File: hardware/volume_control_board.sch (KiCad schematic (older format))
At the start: 39 parts, among them J1 Screw_Terminal_01x08, J2 Audio-Jack-3, J3 Conn_01x04, J4 Conn_01x04, J5 Conn_01x04, J6 RXTX/CAN, SW1 Rotary_Encoder_Switch, U1 Teensy3.2, U2 AD5254

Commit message: finished first draft.
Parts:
- removed J2: Audio-Jack-3, project:BARREL_JACK, symbol volume_control_board-rescue:Audio-Jack-3
- removed SW1: Rotary_Encoder_Switch, Rotary_Encoder:RotaryEncoder_Alps_EC11E-Switch_Vertical_H20mm, symbol volume_control_board-rescue:Rotary_Encoder_Switch
- added J2: AudioJack3, Connector_Audio:Jack_3.5mm_CUI_SJ-3523-SMT_Horizontal, symbol Connector:AudioJack3
- added SW1: Rotary_Encoder_Switch, Rotary_Encoder:RotaryEncoder_Alps_EC11E-Switch_Vertical_H20mm, symbol Device:Rotary_Encoder_Switch
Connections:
- net GND: now also SW1.C, SW1.S2
- net GNDA: now also J2.S
- net LEFT_IN: now also J2.T; no longer J4.1 (Pin_1), U2.1 (W0), U2.2 (B0)
- net RIGHT_IN: now also J2.R; no longer J4.3 (Pin_3), U2.12 (B2), U2.13 (W2)
- net at J3.1 (Pin_1), R4.2, R6.2: now also SW1.A
- net at J3.2 (Pin_2), R5.1, R7.2: now also SW1.B
- net at J3.3 (Pin_3), R8.2, R9.2: now also SW1.S1
- new net: J4.1 (Pin_1), U2.1 (W0), U2.2 (B0)
- new net: J4.3 (Pin_3), U2.12 (B2), U2.13 (W2)
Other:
- moved on the sheet: C5
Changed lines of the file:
@@
-$EndComp
-$Comp
-L volume_control_board-rescue:Rotary_Encoder_Switch SW1
-U 1 1 5C4E5A09
-P 7350 5600
-F 0 "SW1" H 7350 5860 50  0000 C CNN
-F 1 "Rotary_Encoder_Switch" H 7350 5340 50  0000 C CNN
-F 2 "Rotary_Encoder:RotaryEncoder_Alps_EC11E-Switch_Vertical_H20mm" H 7250 5760 50  0001 C CNN
-F 3 "" H 7350 5860 50  0001 C CNN
-	1    7350 5600
-	1    0    0    -1
 $EndComp
 $Comp
@@
 Text Notes 5250 2050 0    59   ~ 0
 Digital Potentiometer
-Text GLabel 8300 4050 0    39   Input ~ 0
+Text GLabel 8800 4150 2    39   Input ~ 0
 RIGHT_IN
-Text GLabel 8300 3950 0    39   Input ~ 0
+Text GLabel 8800 4250 2    39   Input ~ 0
 LEFT_IN
-$Comp
-L volume_control_board-rescue:Audio-Jack-3 J2
-U 1 1 5C526FE2
-P 8600 3950
-F 0 "J2" H 8550 4125 50  0000 C CNN
-F 1 "Audio-Jack-3" H 8700 3850 50  0000 C CNN
-F 2 "project:BARREL_JACK" H 8850 4050 50  0001 C CNN
-F 3 "" H 8850 4050 50  0001 C CNN
-	1    8600 3950
-	-1   0    0    1
-$EndComp
 $Comp
 L volume_control_board-rescue:C C5
 U 1 1 5C527180
-P 9550 3950
-F 0 "C5" H 9575 4050 50  0000 L CNN
-F 1 "0.1uF" H 9575 3850 50  0000 L CNN
-F 2 "Capacitors_SMD:C_0805" H 9588 3800 50  0001 C CNN
-F 3 "" H 9550 3950 50  0001 C CNN
-	1    9550 3950
+P 9500 4150
+F 0 "C5" H 9525 4250 50  0000 L CNN
+F 1 "0.1uF" H 9525 4050 50  0000 L CNN
+F 2 "Capacitors_SMD:C_0805" H 9538 4000 50  0001 C CNN
+F 3 "" H 9500 4150 50  0001 C CNN
+	1    9500 4150
 	1    0    0    -1
 $EndComp
@@
 L power:GND #PWR022
 U 1 1 5C527214
-P 9550 4150
-F 0 "#PWR022" H 9550 3900 50  0001 C CNN
-F 1 "GND" H 9550 4000 50  0000 C CNN
-F 2 "" H 9550 4150 50  0001 C CNN
-F 3 "" H 9550 4150 50  0001 C CNN
-	1    9550 4150
+P 9500 4350
+F 0 "#PWR022" H 9500 4100 50  0001 C CNN
+F 1 "GND" H 9500 4200 50  0000 C CNN
+F 2 "" H 9500 4350 50  0001 C CNN
+F 3 "" H 9500 4350 50  0001 C CNN
+	1    9500 4350
 	1    0    0    -1
 $EndComp
@@
 	4750 2800 4800 2800
 Wire Wire Line
-	8300 4050 8400 4050
-Wire Wire Line
-	8300 3950 8400 3950
-Wire Wire Line
-	9550 4150 9550 4100
+	9500 4350 9500 4300
 Text Notes 8300 3700 0    59   ~ 0
 Audio Signal In
@@
 	6700 2650 6250 2650
 Connection ~ 6250 2650
-Wire Wire Line
-	6600 4150 6600 4050
 Connection ~ 6600 3700
-Wire Wire Line
-	6600 4050 6700 4050
-Wire Wire Line
-	6700 4050 6700 3700
-Connection ~ 6600 4050
-Wire Wire Line
-	6600 4050 6600 3700
-Connection ~ 6700 3700
-Wire Wire Line
-	6400 4150 6400 4050
 Connection ~ 6400 3700
-Wire Wire Line
-	6400 4050 6500 4050
-Wire Wire Line
-	6500 4050 6500 3700
-Connection ~ 6400 4050
-Wire Wire Line
-	6400 4050 6400 3700
-Connection ~ 6500 3700
 Wire Wire Line
 	6900 2800 6900 2450
@@
 L power:GNDA #PWR0105
 U 1 1 5C8C71BF
-P 8800 3850
-F 0 "#PWR0105" H 8800 3600 50  0001 C CNN
-F 1 "GNDA" V 8800 3650 50  0000 C CNN
-F 2 "" H 8800 3850 50  0001 C CNN
-F 3 "" H 8800 3850 50  0001 C CNN
-	1    8800 3850
+P 8800 4050
+F 0 "#PWR0105" H 8800 3800 50  0001 C CNN
+F 1 "GNDA" V 8800 3850 50  0000 C CNN
+F 2 "" H 8800 4050 50  0001 C CNN
+F 3 "" H 8800 4050 50  0001 C CNN
+	1    8800 4050
 	0    -1   -1   0
 $EndComp
@@
 L power:GNDA #PWR0106
 U 1 1 5C8CA019
-P 9550 3800
-F 0 "#PWR0106" H 9550 3550 50  0001 C CNN
-F 1 "GNDA" H 9550 3650 50  0000 C CNN
-F 2 "" H 9550 3800 50  0001 C CNN
-F 3 "" H 9550 3800 50  0001 C CNN
-	1    9550 3800
+P 9500 4000
+F 0 "#PWR0106" H 9500 3750 50  0001 C CNN
+F 1 "GNDA" H 9500 3850 50  0000 C CNN
+F 2 "" H 9500 4000 50  0001 C CNN
+F 3 "" H 9500 4000 50  0001 C CNN
+	1    9500 4000
 	-1   0    0    1
 $EndComp
@@
 Wire Wire Line
 	1400 2700 1300 2700
+$Comp
+L Device:Rotary_Encoder_Switch SW1
+U 1 1 5C9C9DF8
+P 7350 5600
+F 0 "SW1" H 7350 5850 50  0000 C CNN
+F 1 "Rotary_Encoder_Switch" H 7350 5350 50  0000 C CNN
+F 2 "Rotary_Encoder:RotaryEncoder_Alps_EC11E-Switch_Vertical_H20mm" H 7200 5760 50  0001 C CNN
+F 3 "~" H 7350 5860 50  0001 C CNN
+	1    7350 5600
+	1    0    0    -1
+$EndComp
+$Comp
+L Connector:AudioJack3 J2
+U 1 1 5C9D3F0D
+P 8600 4150
+F 0 "J2" H 8580 4475 50  0000 C CNN
+F 1 "AudioJack3" H 8580 4384 50  0000 C CNN
+F 2 "Connector_Audio:Jack_3.5mm_CUI_SJ-3523-SMT_Horizontal" H 8600 4150 50  0001 C CNN
+F 3 "~" H 8600 4150 50  0001 C CNN
+	1    8600 4150
+	1    0    0    -1
+$EndComp
+Wire Wire Line
+	6400 3700 6400 4150
+Wire Wire Line
+	6600 3700 6600 4150
 $EndSCHEMATC

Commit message: firmware v1 and board v2
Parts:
- removed J4, J5: Conn_01x04, Socket_Strips:Socket_Strip_Straight_1x04_Pitch2.54mm, symbol Connector_Generic:Conn_01x04
- added J10, J5, J8, J9: Conn_01x03, Socket_Strips:Socket_Strip_Straight_1x03_Pitch2.00mm, symbol Connector_Generic:Conn_01x03
- added J4: Screw_Terminal_01x02, Socket_Strips:Socket_Strip_Straight_1x02_Pitch2.54mm, symbol Connector:Screw_Terminal_01x02
- added J7: Conn_01x04, Connectors:Grove_1x04, symbol Connector_Generic:Conn_01x04
- J3: footprint Socket_Strips:Socket_Strip_Straight_1x04_Pitch2.54mm -> Connectors:Grove_1x04
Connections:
- net +3V3: now also U1.31 (3.3V_max100mA)
- net +5V: now also J4.1 (Pin_1)
- net FRONT_L_OUT: now also U2.1 (W0), J5.2 (Pin_2); no longer U2.3 (A0)
- net FRONT_R_OUT: now also U2.13 (W2), J9.2 (Pin_2); no longer U2.11 (A2)
- net GND: now also J3.1 (Pin_1), J4.2 (Pin_2), J7.1 (Pin_1); no longer J3.4 (Pin_4)
- net GNDA: now also U2.12 (B2), U2.18 (B3), U2.2 (B0), U2.7 (B1), J10.3 (Pin_3), J5.3 (Pin_3), J8.3 (Pin_3), J9.3 (Pin_3)
- net LEFT_IN: now also U2.3 (A0), U2.8 (A1), J5.1 (Pin_1), J8.1 (Pin_1); no longer U2.6 (W1), U2.7 (B1)
- net REAR_L_OUT: now also U2.6 (W1), J8.2 (Pin_2); no longer U2.8 (A1)
- net REAR_R_OUT: now also U2.19 (W3), J10.2 (Pin_2); no longer U2.17 (A3)
- net RIGHT_IN: now also U2.11 (A2), U2.17 (A3), J10.1 (Pin_1), J9.1 (Pin_1); no longer U2.18 (B3), U2.19 (W3)
- net at R8.2, R9.2, SW1.S1: now also J3.2 (Pin_2), J7.2 (Pin_2); no longer J3.3 (Pin_3)
- net at R4.2, R6.2, SW1.A: now also J3.4 (Pin_4), J7.4 (Pin_4); no longer J3.1 (Pin_1)
- net at R5.1, R7.2, SW1.B: now also J3.3 (Pin_3), J7.3 (Pin_3); no longer J3.2 (Pin_2)
- no-connect marks 34 -> 33
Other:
- note added: "Alt 5V supply"
- note added: "Only populate\none of each to\nselect address"
- moved on the sheet: C1, C5, J1, J2, J3, R10, R11, R12, R13, R3, SW1, U2

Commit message: added a few resistors for adjusting later.
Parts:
- added R14, R15, R16, R17: 10K, Resistors_SMD:R_0805, symbol Device:R
- J4: value Screw_Terminal_01x02 -> 5V in
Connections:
- net LEFT_IN: now also R14.1, R15.1; no longer J5.1 (Pin_1), J8.1 (Pin_1), U2.3 (A0), U2.8 (A1)
- net RIGHT_IN: now also R16.1, R17.1; no longer J10.1 (Pin_1), J9.1 (Pin_1), U2.11 (A2), U2.17 (A3)
- new net: J9.1 (Pin_1), R16.2, U2.11 (A2)
- new net: J10.1 (Pin_1), R17.2, U2.17 (A3)
- new net: J5.1 (Pin_1), R14.2, U2.3 (A0)
- new net: J8.1 (Pin_1), R15.2, U2.8 (A1)
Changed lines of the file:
@@
 Text GLabel 1200 4600 1    39   Input ~ 0
 SDA
-Text GLabel 7200 2750 2    39   Input ~ 0
+Text GLabel 7500 2750 2    39   Input ~ 0
 LEFT_IN
-Text GLabel 7200 3550 2    39   Input ~ 0
+Text GLabel 7500 3550 2    39   Input ~ 0
 RIGHT_IN
 $Comp
@@
 	0    -1   -1   0
 $EndComp
-Text GLabel 7200 3150 2    39   Input ~ 0
+Text GLabel 7500 3150 2    39   Input ~ 0
 RIGHT_IN
-Text GLabel 7200 2350 2    39   Input ~ 0
+Text GLabel 7500 2350 2    39   Input ~ 0
 LEFT_IN
 Wire Wire Line
@@
 U 1 1 5CB5DB64
 P 4350 1400
-F 0 "J4" V 4350 1550 50  0000 R CNN
-F 1 "Screw_Terminal_01x02" H 4400 1200 50  0000 R CNN
+F 0 "J4" H 4400 1500 50  0000 R CNN
+F 1 "5V in" H 4400 1200 50  0000 R CNN
 F 2 "Socket_Strips:Socket_Strip_Straight_1x02_Pitch2.54mm" H 4350 1400 50  0001 C CNN
 F 3 "~" H 4350 1400 50  0001 C CNN
@@
 Alt 5V supply
 Connection ~ 5250 2450
+$Comp
+L Device:R R14
+U 1 1 5CBA3FFB
+P 7350 2350
+F 0 "R14" V 7250 2350 50  0000 C CNN
+F 1 "10K" V 7350 2350 50  0000 C CNN
+F 2 "Resistors_SMD:R_0805" V 7280 2350 50  0001 C CNN
+F 3 "~" H 7350 2350 50  0001 C CNN
+	1    7350 2350
+	0    1    1    0
+$EndComp
+$Comp
+L Device:R R15
+U 1 1 5CBA43B6
+P 7350 2750
+F 0 "R15" V 7250 2750 50  0000 C CNN
+F 1 "10K" V 7350 2750 50  0000 C CNN
+F 2 "Resistors_SMD:R_0805" V 7280 2750 50  0001 C CNN
+F 3 "~" H 7350 2750 50  0001 C CNN
+	1    7350 2750
+	0    1    1    0
+$EndComp
+$Comp
+L Device:R R16
+U 1 1 5CBA4434
+P 7350 3150
+F 0 "R16" V 7250 3150 50  0000 C CNN
+F 1 "10K" V 7350 3150 50  0000 C CNN
+F 2 "Resistors_SMD:R_0805" V 7280 3150 50  0001 C CNN
+F 3 "~" H 7350 3150 50  0001 C CNN
+	1    7350 3150
+	0    1    1    0
+$EndComp
+$Comp
+L Device:R R17
+U 1 1 5CBA44B0
+P 7350 3550
+F 0 "R17" V 7250 3550 50  0000 C CNN
+F 1 "10K" V 7350 3550 50  0000 C CNN
+F 2 "Resistors_SMD:R_0805" V 7280 3550 50  0001 C CNN
+F 3 "~" H 7350 3550 50  0001 C CNN
+	1    7350 3550
+	0    1    1    0
+$EndComp
 $EndSCHEMATC

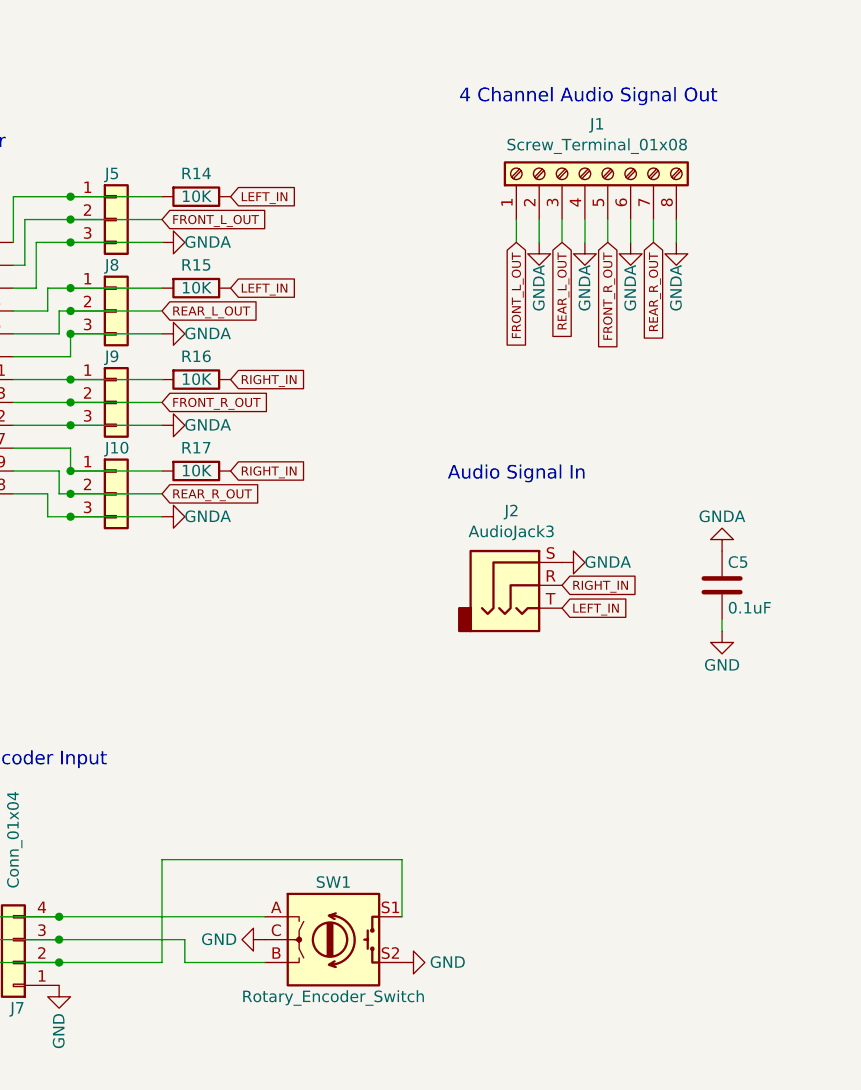
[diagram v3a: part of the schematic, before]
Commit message: updated board with more breakouts.
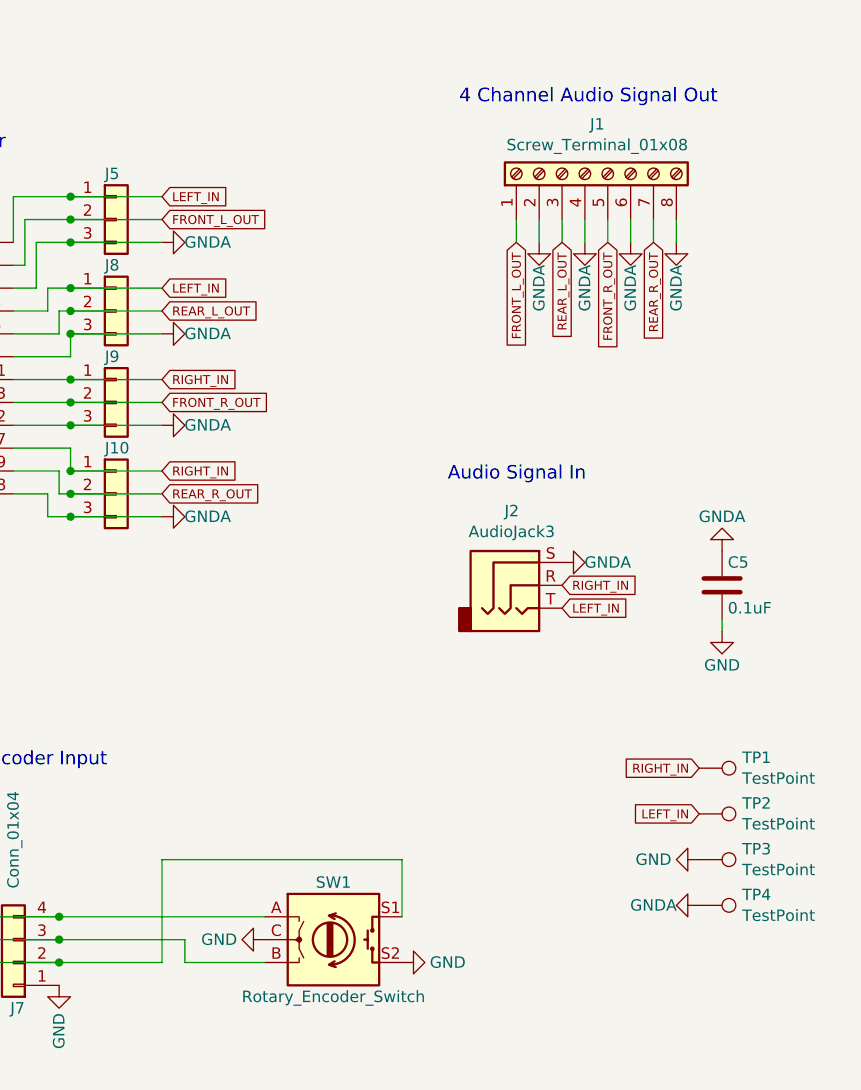
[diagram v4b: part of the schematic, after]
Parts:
- removed R14, R15, R16, R17: 10K, Resistors_SMD:R_0805, symbol Device:R
- added TP1, TP2, TP3, TP4: TestPoint, Measurement_Points:Measurement_Point_Round-TH_Small, symbol Connector:TestPoint
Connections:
- net GND: now also TP3.1
- net GNDA: now also TP4.1
- net LEFT_IN: now also J5.1 (Pin_1), J8.1 (Pin_1), U2.3 (A0), U2.8 (A1), TP2.1
- net RIGHT_IN: now also J10.1 (Pin_1), J9.1 (Pin_1), U2.11 (A2), U2.17 (A3), TP1.1
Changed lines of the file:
@@
 Text GLabel 1200 4600 1    39   Input ~ 0
 SDA
-Text GLabel 7500 2750 2    39   Input ~ 0
+Text GLabel 7200 2750 2    39   Input ~ 0
 LEFT_IN
-Text GLabel 7500 3550 2    39   Input ~ 0
+Text GLabel 7200 3550 2    39   Input ~ 0
 RIGHT_IN
 $Comp
@@
 	0    -1   -1   0
 $EndComp
-Text GLabel 7500 3150 2    39   Input ~ 0
+Text GLabel 7200 3150 2    39   Input ~ 0
 RIGHT_IN
-Text GLabel 7500 2350 2    39   Input ~ 0
+Text GLabel 7200 2350 2    39   Input ~ 0
 LEFT_IN
 Wire Wire Line
@@
 Connection ~ 5250 2450
 $Comp
-L Device:R R14
-U 1 1 5CBA3FFB
-P 7350 2350
-F 0 "R14" V 7250 2350 50  0000 C CNN
-F 1 "10K" V 7350 2350 50  0000 C CNN
-F 2 "Resistors_SMD:R_0805" V 7280 2350 50  0001 C CNN
-F 3 "~" H 7350 2350 50  0001 C CNN
-	1    7350 2350
-	0    1    1    0
-$EndComp
-$Comp
-L Device:R R15
-U 1 1 5CBA43B6
-P 7350 2750
-F 0 "R15" V 7250 2750 50  0000 C CNN
-F 1 "10K" V 7350 2750 50  0000 C CNN
-F 2 "Resistors_SMD:R_0805" V 7280 2750 50  0001 C CNN
-F 3 "~" H 7350 2750 50  0001 C CNN
-	1    7350 2750
-	0    1    1    0
-$EndComp
-$Comp
-L Device:R R16
-U 1 1 5CBA4434
-P 7350 3150
-F 0 "R16" V 7250 3150 50  0000 C CNN
-F 1 "10K" V 7350 3150 50  0000 C CNN
-F 2 "Resistors_SMD:R_0805" V 7280 3150 50  0001 C CNN
-F 3 "~" H 7350 3150 50  0001 C CNN
-	1    7350 3150
-	0    1    1    0
-$EndComp
-$Comp
-L Device:R R17
-U 1 1 5CBA44B0
-P 7350 3550
-F 0 "R17" V 7250 3550 50  0000 C CNN
-F 1 "10K" V 7350 3550 50  0000 C CNN
-F 2 "Resistors_SMD:R_0805" V 7280 3550 50  0001 C CNN
-F 3 "~" H 7350 3550 50  0001 C CNN
-	1    7350 3550
-	0    1    1    0
-$EndComp
+L Connector:TestPoint TP1
+U 1 1 5CB5708F
+P 9550 4850
+F 0 "TP1" V 9504 5038 50  0000 L CNN
+F 1 "TestPoint" V 9595 5038 50  0000 L CNN
+F 2 "Measurement_Points:Measurement_Point_Round-TH_Small" H 9750 4850 50  0001 C CNN
+F 3 "~" H 9750 4850 50  0001 C CNN
+	1    9550 4850
+	0    1    1    0
+$EndComp
+$Comp
+L Connector:TestPoint TP2
+U 1 1 5CB57244
+P 9550 5050
+F 0 "TP2" V 9504 5238 50  0000 L CNN
+F 1 "TestPoint" V 9595 5238 50  0000 L CNN
+F 2 "Measurement_Points:Measurement_Point_Round-TH_Small" H 9750 5050 50  0001 C CNN
+F 3 "~" H 9750 5050 50  0001 C CNN
+	1    9550 5050
+	0    1    1    0
+$EndComp
+$Comp
+L Connector:TestPoint TP3
+U 1 1 5CB572D0
+P 9550 5250
+F 0 "TP3" V 9504 5438 50  0000 L CNN
+F 1 "TestPoint" V 9595 5438 50  0000 L CNN
+F 2 "Measurement_Points:Measurement_Point_Round-TH_Small" H 9750 5250 50  0001 C CNN
+F 3 "~" H 9750 5250 50  0001 C CNN
+	1    9550 5250
+	0    1    1    0
+$EndComp
+$Comp
+L Connector:TestPoint TP4
+U 1 1 5CB57348
+P 9550 5450
+F 0 "TP4" V 9504 5638 50  0000 L CNN
+F 1 "TestPoint" V 9595 5638 50  0000 L CNN
+F 2 "Measurement_Points:Measurement_Point_Round-TH_Small" H 9750 5450 50  0001 C CNN
+F 3 "~" H 9750 5450 50  0001 C CNN
+	1    9550 5450
+	0    1    1    0
+$EndComp
+Text GLabel 9550 4850 0    39   Input ~ 0
+RIGHT_IN
+Text GLabel 9550 5050 0    39   Input ~ 0
+LEFT_IN
+$Comp
+L power:GND #PWR0120
+U 1 1 5CB5773E
+P 9550 5250
+F 0 "#PWR0120" H 9550 5000 50  0001 C CNN
+F 1 "GND" V 9550 5050 50  0000 C CNN
+F 2 "" H 9550 5250 50  0001 C CNN
+F 3 "" H 9550 5250 50  0001 C CNN
+	1    9550 5250
+	0    1    1    0
+$EndComp
+$Comp
+L power:GNDA #PWR0121
+U 1 1 5CB577D9
+P 9550 5450
+F 0 "#PWR0121" H 9550 5200 50  0001 C CNN
+F 1 "GNDA" V 9550 5250 50  0000 C CNN
+F 2 "" H 9550 5450 50  0001 C CNN
+F 3 "" H 9550 5450 50  0001 C CNN
+	1    9550 5450
+	0    1    1    0
+$EndComp
